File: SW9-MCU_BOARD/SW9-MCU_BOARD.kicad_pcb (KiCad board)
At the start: 2 copper layers, 2 parts, among them IC1 STM32L051C6T6, U1 STM32L051C6Tx

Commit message: update stuff
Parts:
- removed U1: STM32L051C6Tx, Package_QFP:LQFP-48_7x7mm_P0.5mm
- added C1: 10pF, Capacitor_SMD:C_0603_1608Metric_Pad1.08x0.95mm_HandSolder, F.Cu at (121.9, 63.9)
- added C10: 100nF, Capacitor_SMD:C_0603_1608Metric_Pad1.08x0.95mm_HandSolder, F.Cu at (127.6, 52.7)
- added C11: 4.7uF, Capacitor_SMD:C_0603_1608Metric_Pad1.08x0.95mm_HandSolder, F.Cu at (125.7, 52.7)
- added C2: 10pF, Capacitor_SMD:C_0603_1608Metric_Pad1.08x0.95mm_HandSolder, F.Cu at (121.9, 60.3)
- added C3: 20pF, Capacitor_SMD:C_0603_1608Metric_Pad1.08x0.95mm_HandSolder, F.Cu at (123.2, 79.8)
- added C4: 20pF, Capacitor_SMD:C_0603_1608Metric_Pad1.08x0.95mm_HandSolder, F.Cu at (125.7, 73.4)
- added C5: 100nF, Capacitor_SMD:C_0603_1608Metric_Pad1.08x0.95mm_HandSolder, F.Cu at (132.0, 76.6)
- added C6: 1uF, Capacitor_SMD:C_0603_1608Metric_Pad1.08x0.95mm_HandSolder, F.Cu at (135.3, 69.4)
- added C7: 10nF, Capacitor_SMD:C_0603_1608Metric_Pad1.08x0.95mm_HandSolder, F.Cu at (137.2, 69.4)
- added C8: 100nF, Capacitor_SMD:C_0603_1608Metric_Pad1.08x0.95mm_HandSolder, F.Cu at (144.8, 67.1)
- added C9: 100nF, Capacitor_SMD:C_0603_1608Metric_Pad1.08x0.95mm_HandSolder, F.Cu at (142.9, 66.9)
- added FB1: FerriteBead, Ferrite_THT:LairdTech_28C0236-0JW-10, F.Cu at (144.1, 75.6)
- added J1: Conn_ARM_JTAG_SWD_10, Connector_PinSocket_2.00mm:PinSocket_1x10_P2.00mm_Vertical, F.Cu at (127.8, 46.4)
- added R1: 390, Resistor_SMD:R_0603_1608Metric_Pad0.98x0.95mm_HandSolder, F.Cu at (123.2, 73.4)
- added R2: 10k, Resistor_SMD:R_0603_1608Metric_Pad0.98x0.95mm_HandSolder, F.Cu at (140.3, 57.8)
- added SW1: SW_DPDT_x2, Button_Switch_SMD:SW_DPDT_CK_JS202011JCQN, F.Cu at (137.2, 49.5)
- added SW2: SW_Push, Button_Switch_THT:SW_Push_2P2T_Toggle_CK_PVA2OAH5xxxxxxV2, F.Cu at (129.5, 81.3)
- added Y1: 32KHz, SWLib:X_ABS25_ABR, F.Cu at (115.6, 76.4)
- added Y2: 8MHz, SWLib:830003151, F.Cu at (116.8, 61.6)
- moved IC1 35.6 mm to (131.9, 61.8)
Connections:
- IC1 pad 1: unconnected-(IC1-VDD_1-Pad1) -> VDD
- IC1 pad 23: unconnected-(IC1-VSS_1-Pad23) -> Earth
- IC1 pad 24: unconnected-(IC1-VDD_2-Pad24) -> VDD
- IC1 pad 3: unconnected-(IC1-PC14-OSC32_IN-Pad3) -> Net-(IC1-PC14-OSC32_IN)
- IC1 pad 34: unconnected-(IC1-PA13-Pad34) -> SWDIO/TMS
- IC1 pad 35: unconnected-(IC1-VSS_2-Pad35) -> Earth
- IC1 pad 37: unconnected-(IC1-PA14-Pad37) -> SWCLK/TCK
- IC1 pad 4: unconnected-(IC1-PC15-OSC32_OUT-Pad4) -> Net-(IC1-PC15-OSC32_OUT)
- IC1 pad 44: unconnected-(IC1-BOOT0-Pad44) -> Net-(IC1-BOOT0)
- IC1 pad 47: unconnected-(IC1-VSS_3-Pad47) -> Earth
- IC1 pad 5: unconnected-(IC1-PH0-OSC_IN-Pad5) -> Net-(IC1-PH0-OSC_IN)
- IC1 pad 6: unconnected-(IC1-PH1-OSC_OUT-Pad6) -> Net-(IC1-PH1-OSC_OUT)
- IC1 pad 7: unconnected-(IC1-NRST-Pad7) -> Net-(IC1-NRST)
- IC1 pad 9: unconnected-(IC1-VDDA-Pad9) -> VDDA

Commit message: layout
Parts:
- moved C8 24.4 mm to (122.6, 57.1), turned to 90 degrees
- moved FB1 22.9 mm to (144.8, 52.7), turned to 0 degrees
- moved C6 10.3 mm to (125.0, 69.3), turned to -90 degrees
- moved R1 9.85 mm to (113.6, 75.8)
- moved C4 9.75 mm to (116.0, 73.4), turned to 0 degrees
- moved C5 9.36 mm to (141.2, 78.1)
- moved SW2 7.76 mm to (127.1, 73.9)
- moved C2 7.67 mm to (114.9, 57.1)
- moved C1 7.67 mm to (114.9, 60.7)
- moved Y2 7.67 mm to (109.9, 58.4)
- moved C7 7.61 mm to (142.2, 63.7)
- moved C9 7.24 mm to (138.4, 72.6)
- moved C3 5.74 mm to (118.5, 76.5), turned to 180 degrees
- moved Y1 5.05 mm to (116.4, 81.4), turned to -90 degrees
- turned R2 to 90 degrees
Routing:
- net Earth: track 0.00 -> 94.5 mm, vias 0 -> 6
- net Net-(IC1-PH0-OSC_IN): track 0.00 -> 42.7 mm
- net Net-(IC1-PH1-OSC_OUT): track 0.00 -> 33.1 mm
- net VDD: track 0.00 -> 12.2 mm
- net Net-(C4-Pad1): track 0.00 -> 2.55 mm
- net (no net): track 0.00 -> 0.51 mm
- added copper zone on B.Cu, net Earth

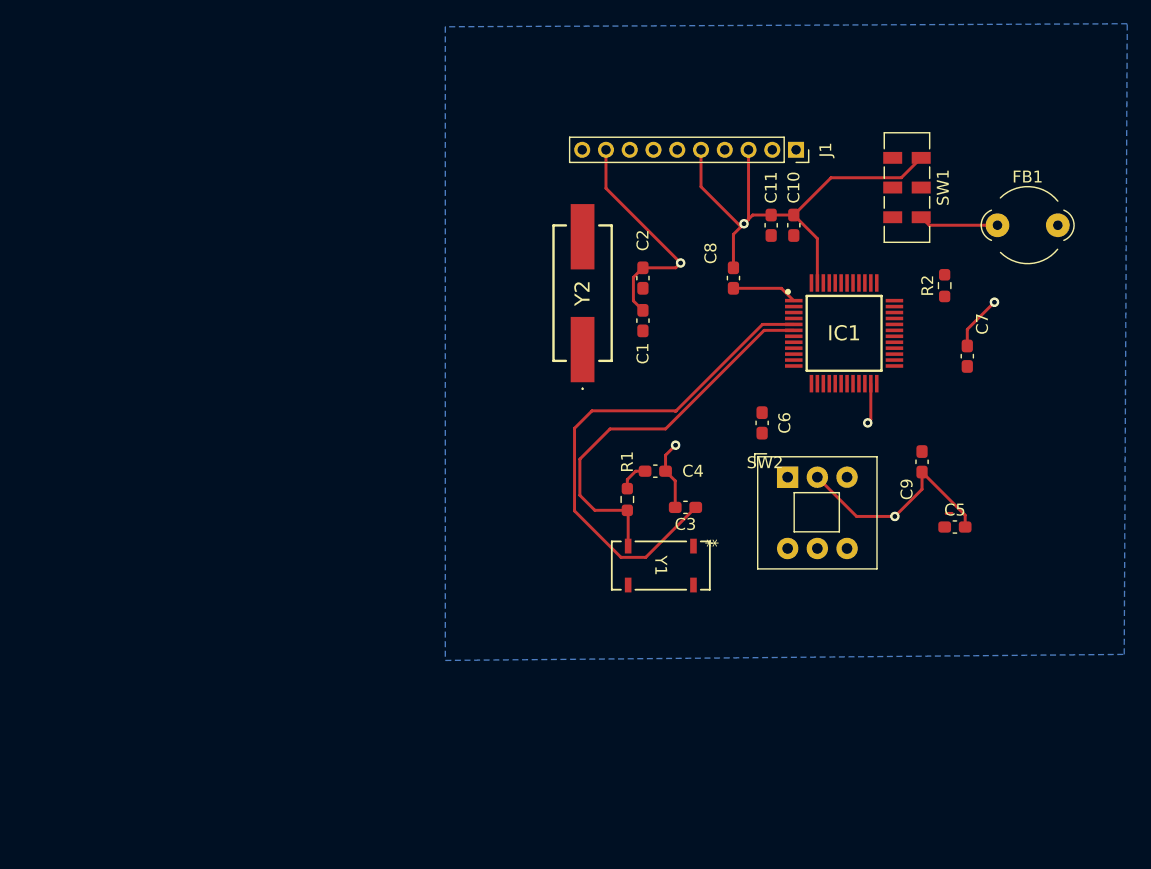
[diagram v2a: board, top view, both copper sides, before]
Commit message: change footprints for oscillators
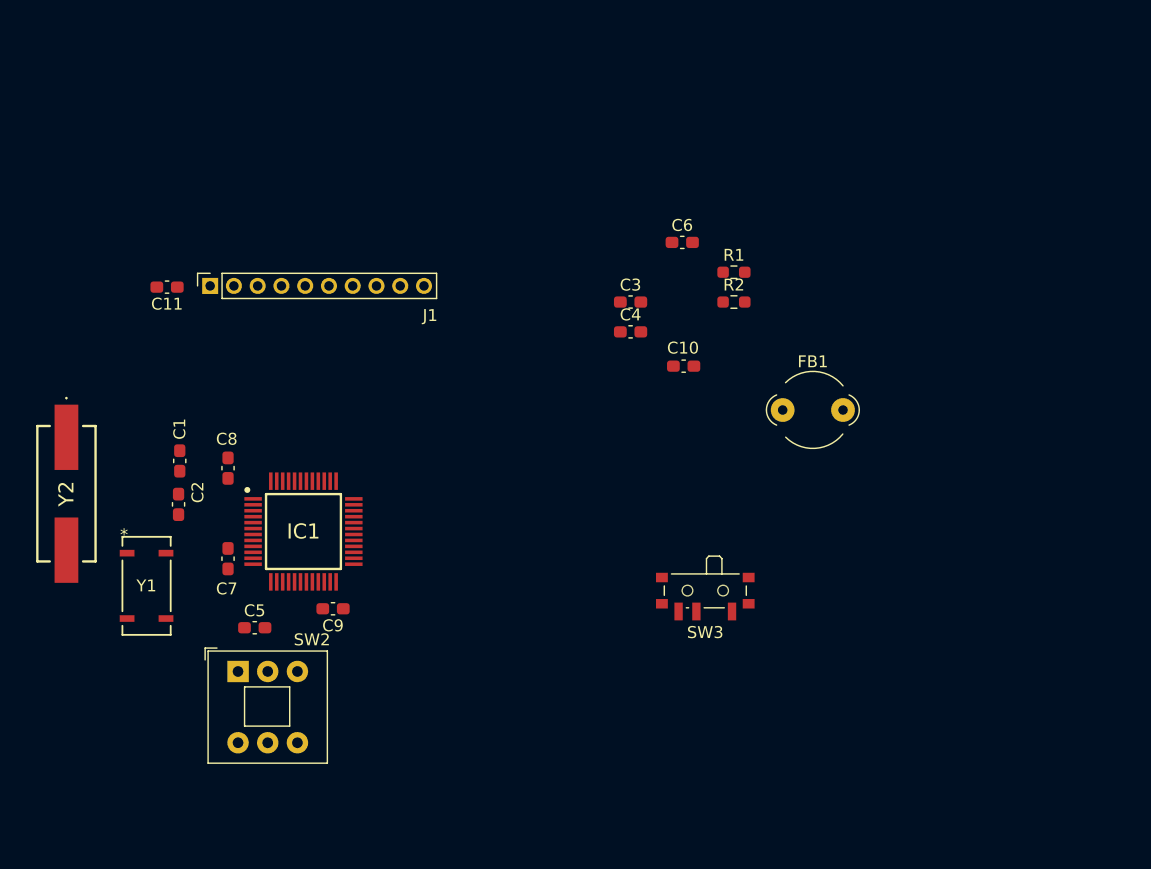
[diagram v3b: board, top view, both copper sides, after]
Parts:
- removed SW1: SW_DPDT_x2, Button_Switch_SMD:SW_DPDT_CK_JS202011JCQN
- added SW3: SW_SPDT, Button_Switch_SMD:SW_SPDT_PCM12, F.Cu at (120.2, 83.8)
- Y1: value 32KHz -> ABS25-32.768KHZ-6-T
- moved C7 64.5 mm to (80.0, 80.8), turned to -90 degrees
- moved C5 59.5 mm to (82.3, 86.6)
- moved C11 51.1 mm to (74.9, 57.9), turned to 180 degrees
- moved C9 51.1 mm to (88.8, 85.0), turned to 180 degrees
- moved J1 50.6 mm to (78.5, 57.8), turned to 90 degrees
- moved SW2 49.1 mm to (80.9, 90.3)
- moved IC1 48.5 mm to (86.4, 78.5)
- moved Y2 46.6 mm to (66.4, 75.3), turned to -90 degrees
- moved C8 45.5 mm to (80.0, 73.2)
- moved C2 43.5 mm to (75.8, 76.2)
- moved Y1 43.3 mm to (73.2, 83.1), turned to 0 degrees
- moved C1 40.7 mm to (75.9, 72.5), turned to -90 degrees
- moved FB1 23.9 mm to (126.7, 68.3)
- moved R1 21.1 mm to (122.6, 56.7), turned to 0 degrees
- moved C3 17.9 mm to (113.9, 59.2), turned to 0 degrees
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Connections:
- Y1 pad 2: Net-(IC1-PH1-OSC_OUT) -> unconnected-(Y1-NC-Pad2)
- Y1 pad 3: (no net) -> unconnected-(Y1-NC-Pad3)
- Y1 pad 4: (no net) -> Net-(IC1-PH1-OSC_OUT)
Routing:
- net Earth: track 94.5 -> 0.00 mm, vias 6 -> 0
- net Net-(IC1-PH0-OSC_IN): track 42.7 -> 0.00 mm
- net Net-(IC1-PH1-OSC_OUT): track 33.1 -> 0.00 mm
- net VDD: track 12.2 -> 0.00 mm
- net Net-(C4-Pad1): track 2.55 -> 0.00 mm
- net (no net): track 0.51 -> 0.00 mm
- removed copper zone on B.Cu, net Earth

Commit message: some changes ig???
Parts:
- removed the C10 at (118.4, 64.6)
- FB1: footprint Ferrite_THT:LairdTech_28C0236-0JW-10 -> Inductor_SMD:L_0201_0603Metric_Pad0.64x0.40mm_HandSolder
- moved R1 58.2 mm to (74.7, 89.7), turned to -90 degrees
- moved C3 54.3 mm to (69.1, 89.8), turned to -90 degrees
- moved C4 51.1 mm to (71.9, 90.7), turned to 180 degrees
- moved FB1 49.4 mm to (78.0, 76.5), turned to -90 degrees
- moved SW3 44.7 mm to (80.7, 63.0)
- moved R2 38.3 mm to (85.9, 70.0), turned to 90 degrees
- moved C10 37.3 mm to (96.1, 88.5), turned to -90 degrees
- moved J1 31.5 mm to (96.0, 84.0), turned to 180 degrees
- moved C6 25.3 mm to (93.0, 55.9), turned to -90 degrees
- moved C1 3.05 mm to (72.9, 72.7)
- moved C2 3.05 mm to (72.8, 76.4)
- renumbered C11 to C10
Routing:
- net VDD: track 0.00 -> 23.2 mm
- net Net-(IC1-PC14-OSC32_IN): track 0.00 -> 18.3 mm
- net Net-(IC1-PH0-OSC_IN): track 0.00 -> 18.1 mm
- net Net-(IC1-PH1-OSC_OUT): track 0.00 -> 17.4 mm
- net Net-(IC1-PC15-OSC32_OUT): track 0.00 -> 17.2 mm
- net Earth: track 0.00 -> 12.6 mm, vias 0 -> 1
- net Net-(SW3-B): track 0.00 -> 7.84 mm
- net Net-(IC1-NRST): track 0.00 -> 3.91 mm
- net Net-(IC1-BOOT0): track 0.00 -> 3.48 mm
- net Net-(C4-Pad1): track 0.00 -> 1.97 mm
- net (no net): vias 0 -> 1
- added copper zone on In1.Cu, net Earth
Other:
- copper layers 2 -> 4

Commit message: more routing
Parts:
- moved C6 22.3 mm to (71.6, 62.5)
- moved FB1 5.69 mm to (77.7, 82.1), turned to 90 degrees
- moved J1 3.05 mm to (99.1, 84.2)
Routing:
- net Earth: track 12.6 -> 56.9 mm, vias 1 -> 7
- net Net-(IC1-NRST): track 3.91 -> 35.5 mm
- net SWCLK/TCK: track 0.00 -> 11.5 mm
- net VDD: track 23.2 -> 30.3 mm, vias 0 -> 2
- net VDDA: track 0.00 -> 5.23 mm
- net Net-(IC1-PH0-OSC_IN): track 18.1 -> 21.3 mm
- net (no net): vias 1 -> 0

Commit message: first layout done
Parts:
- removed C7: 10nF, Capacitor_SMD:C_0603_1608Metric_Pad1.08x0.95mm_HandSolder
- moved C6 21.6 mm to (79.8, 82.5)
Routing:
- net Earth: track 56.9 -> 82.1 mm, vias 7 -> 8
- net SWDIO/TMS: track 0.00 -> 10.7 mm
- net SWCLK/TCK: track 11.5 -> 14.9 mm, vias 0 -> 1
- net Net-(IC1-NRST): track 35.5 -> 38.5 mm
- net VDDA: track 5.23 -> 6.12 mm
- added copper zone on In2.Cu, net VDD
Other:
- board outline added: 38.1 x 37.5 mm
